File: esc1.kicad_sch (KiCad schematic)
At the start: 91 parts, among them J2 Phase Outputs, J3 Pad Terminals, J4 Signal, U1 IRS21867S, U13 STM32F303CBTx, U4 INA180A3, U6 IRS21867S, U7 IRS21867S, U8 INA180A3, U9 INA180A3

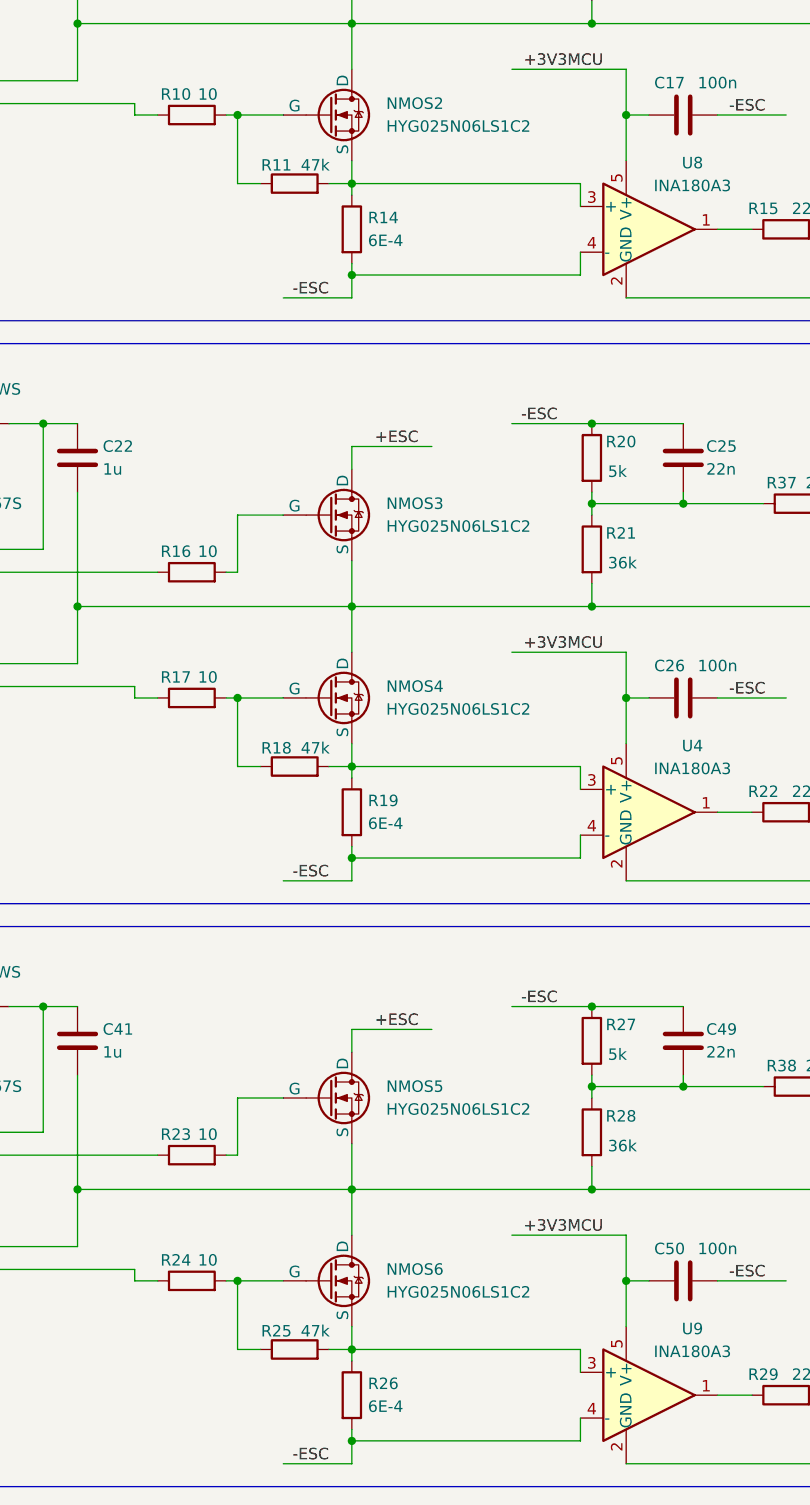
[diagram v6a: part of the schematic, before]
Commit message: Routing Update. Signal powers routed except for MCU. Look for unrouted traces without vias. Vias for signal lines added for organization
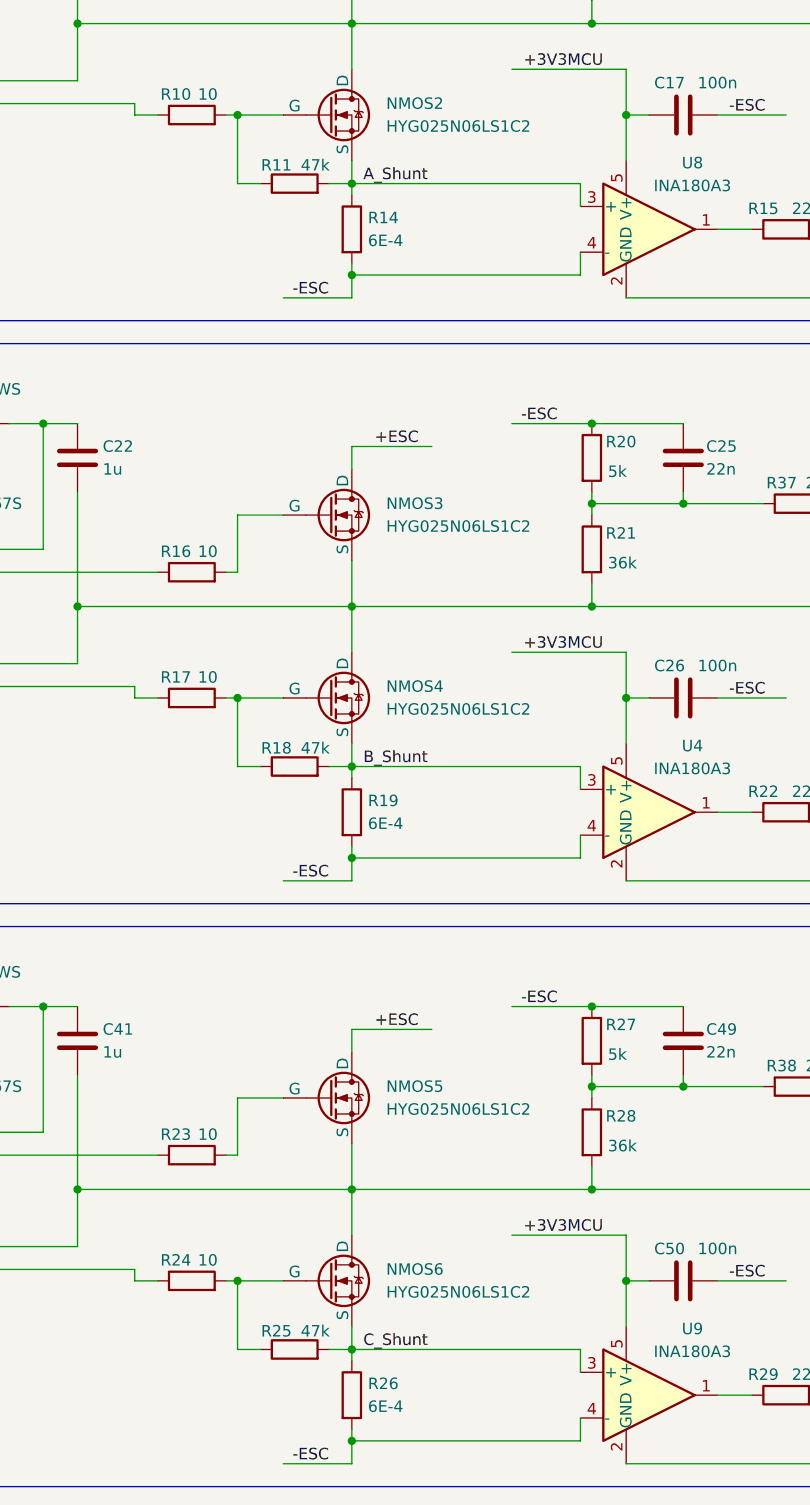
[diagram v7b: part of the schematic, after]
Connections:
- net A_Shunt: now reaches NMOS2.3 (S), R11.2, R14.1, U8.3 (+)
- net B_Shunt: now reaches NMOS4.3 (S), R18.2, R19.1, U4.3 (+)
- net C_Shunt: now reaches NMOS6.3 (S), R25.2, R26.1, U9.3 (+)
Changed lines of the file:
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@@
+		)
+	)
+	(label "C_Shunt"
+		(at 279.4 195.58 0)
+		(effects
+			(font
+				(size 1.27 1.27)
+			)
+			(justify left bottom)
 		)
 	)
@@
 		)
 	)
+	(label "B_Shunt"
+		(at 279.4 130.81 0)
+		(effects
+			(font
+				(size 1.27 1.27)
+			)
+			(justify left bottom)
+		)
+	)
 	(label "-3V3MCU"
 		(at 171.45 72.39 0)
@@
 		)
 	)
+	(label "A_Shunt"
+		(at 279.4 66.04 0)
+		(effects
+			(font
+				(size 1.27 1.27)
+			)
+			(justify left bottom)
+		)
+	)

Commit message: Update Type stuff
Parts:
- removed C17, C50: 100n, easyeda2kicad:C0805, symbol Device:C
- removed C18, C51: 22n, Capacitor_SMD:C_0805_2012Metric, symbol Device:C
- removed R14: 6E-4, easyeda2kicad:RES-SMD_L6.4-W3.2_LRS2512, symbol Device:R
- removed R15: 220, easyeda2kicad:R0805, symbol Device:R
- removed U8: INA180A3, Package_TO_SOT_SMD:SOT-23-5, symbol Amplifier_Current:INA180A3
- added C29: 100n, easyeda2kicad:C0805, symbol Device:C
- added C40: 22n, Capacitor_SMD:C_0805_2012Metric, symbol Device:C
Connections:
- net +3V3MCU: now also C29.1
- net -ESC: now also NMOS4.3 (S), R18.2, C29.2
- net MCU_AI: now also R29.2, C40.1
- net MCU_CI: now also C27.1, R22.2; no longer R29.2
- net at U9.2 (GND): now also C40.2
- net A_Shunt renamed Shunt_A
- net Shunt_A: now also R26.1, U9.3 (+)
- net B_Shunt renamed Shunt_C
- net Shunt_C: now also NMOS6.3 (S), R25.2; no longer NMOS4.3 (S), R18.2
- removed net C_Shunt: NMOS6.3 (S), R25.2, R26.1, U9.3 (+)
- removed net MCU_BI: C27.1, R22.2, U13.26 (PB13)
- no-connect marks 21 -> 22
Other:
- note removed: "ADC4_CH5"
- moved on the sheet: C20, C21, C22, C25, D10, NMOS3, NMOS4, R16, R17, R18, R20, R21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
